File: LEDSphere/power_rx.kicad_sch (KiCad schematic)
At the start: 46 parts, among them U10 DRV5032FCDBZR, U3 TPS54202HDDCR, U4 TPS54202HDDCR

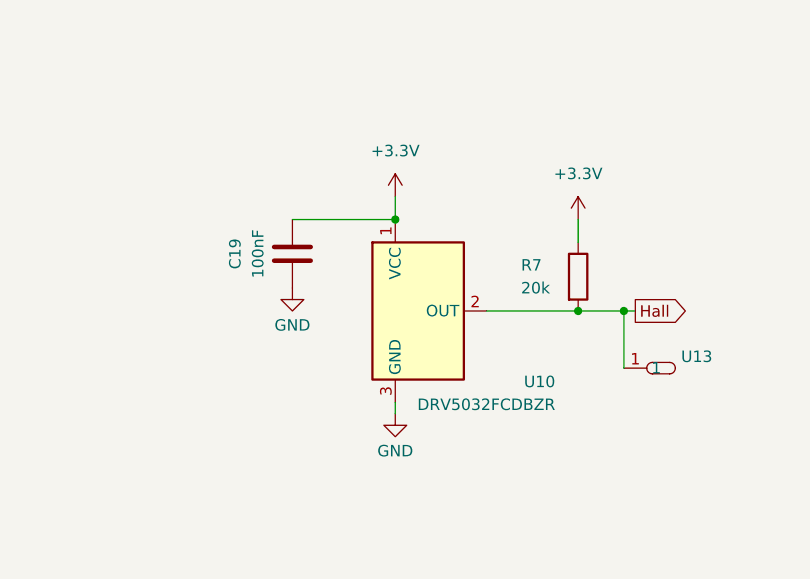
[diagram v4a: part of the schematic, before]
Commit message: change hall effect sensor
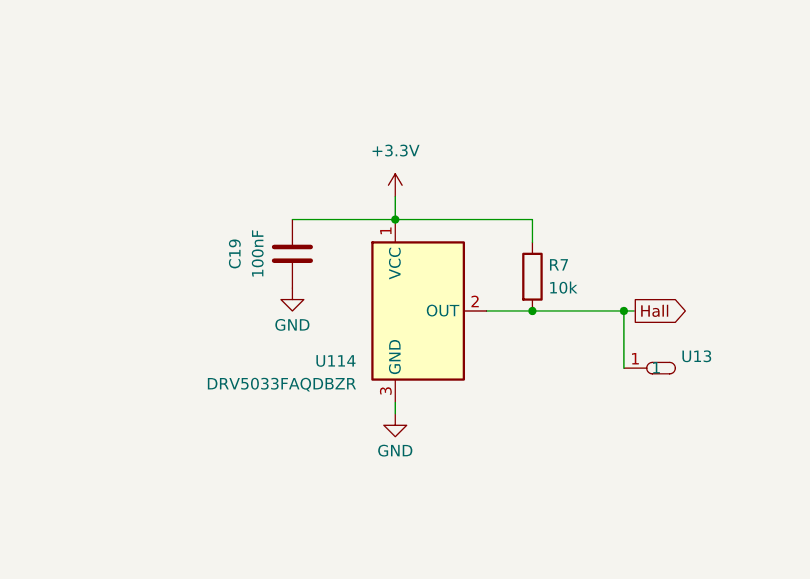
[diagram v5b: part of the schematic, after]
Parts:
- removed U10: DRV5032FCDBZR, Package_TO_SOT_SMD:SOT-23, symbol Sensor_Magnetic:DRV5033AJxDBZ
- added U114: DRV5033FAQDBZR, Package_TO_SOT_SMD:SOT-23-3, symbol Sensor_Magnetic:DRV5033FAxDBZ
- R7: value 20k -> 10k
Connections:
- net +3.3V: now also U114.1 (VCC)
- net GND: now also U114.3 (GND)
- net Hall: now also U114.2 (OUT)
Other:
- moved on the sheet: R7
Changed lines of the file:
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@@
 	)
 	(junction
+		(at 242.57 121.92)
+		(diameter 0)
+		(color 0 0 0 0)
+	)
+	(junction
 		(at 85.09 50.8)
 		(diameter 0)
@@
 	)
 	(junction
-		(at 247.65 121.92)
-		(diameter 0)
-		(color 0 0 0 0)
-	)
-	(junction
 		(at 158.75 162.56)
 		(diameter 0)
@@
 	(wire
 		(pts
+			(xy 237.49 121.92) (xy 242.57 121.92)
+		)
+		(stroke
+			(width 0)
+			(type default)
+		)
+	)
+	(wire
+		(pts
 			(xy 166.37 161.29) (xy 166.37 162.56)
 		)
@@
 	(wire
 		(pts
-			(xy 247.65 121.92) (xy 252.73 121.92)
+			(xy 99.06 52.07) (xy 81.28 52.07)
 		)
 		(stroke
@@
 	(wire
 		(pts
-			(xy 99.06 52.07) (xy 81.28 52.07)
+			(xy 99.06 50.8) (xy 99.06 52.07)
 		)
 		(stroke
@@
 	(wire
 		(pts
-			(xy 99.06 50.8) (xy 99.06 52.07)
+			(xy 227.33 109.22) (xy 227.33 111.76)
 		)
 		(stroke
@@
 	(wire
 		(pts
-			(xy 227.33 109.22) (xy 227.33 111.76)
+			(xy 227.33 111.76) (xy 242.57 111.76)
 		)
 		(stroke
@@
 	(wire
 		(pts
-			(xy 123.19 54.61) (xy 123.19 60.96)
+			(xy 242.57 121.92) (xy 252.73 121.92)
 		)
 		(stroke
@@
 	(wire
 		(pts
-			(xy 227.33 133.35) (xy 227.33 132.08)
+			(xy 123.19 54.61) (xy 123.19 60.96)
 		)
 		(stroke
@@
 	(wire
 		(pts
-			(xy 142.24 115.57) (xy 138.43 115.57)
+			(xy 227.33 133.35) (xy 227.33 132.08)
 		)
 		(stroke
@@
 	(wire
 		(pts
-			(xy 165.1 106.68) (xy 165.1 114.3)
+			(xy 142.24 115.57) (xy 138.43 115.57)
 		)
 		(stroke
@@
 	(wire
 		(pts
-			(xy 45.72 154.94) (xy 59.69 154.94)
+			(xy 165.1 106.68) (xy 165.1 114.3)
 		)
 		(stroke
@@
 	(wire
 		(pts
-			(xy 139.7 171.45) (xy 139.7 170.18)
+			(xy 45.72 154.94) (xy 59.69 154.94)
 		)
 		(stroke
@@
 	(wire
 		(pts
-			(xy 123.19 43.18) (xy 123.19 46.99)
+			(xy 139.7 171.45) (xy 139.7 170.18)
 		)
 		(stroke
@@
 	(wire
 		(pts
-			(xy 252.73 121.92) (xy 254 121.92)
+			(xy 123.19 43.18) (xy 123.19 46.99)
 		)
 		(stroke
@@
 	(wire
 		(pts
-			(xy 237.49 121.92) (xy 247.65 121.92)
+			(xy 252.73 121.92) (xy 254 121.92)
 		)
 		(stroke
@@
 	(wire
 		(pts
-			(xy 247.65 111.76) (xy 247.65 114.3)
+			(xy 242.57 111.76) (xy 242.57 114.3)
 		)
 		(stroke
@@
 	(symbol
 		(lib_id "Device:R")
-		(at 247.65 118.11 0)
+		(at 242.57 118.11 0)
 		(unit 1)
 		(body_style 1)
@@
 		(dnp no)
 		(property "Reference" "R7"
-			(at 241.3 116.84 0)
+			(at 244.348 116.84 0)
 			(show_name no)
 			(do_not_autoplace no)
@@
 			)
 		)
-		(property "Value" "20k"
-			(at 241.3 119.38 0)
+		(property "Value" "10k"
+			(at 244.348 119.38 0)
 			(show_name no)
 			(do_not_autoplace no)
@@
 		)
 		(property "Footprint" "Resistor_SMD:R_0603_1608Metric"
-			(at 245.872 118.11 90)
+			(at 240.792 118.11 90)
 			(hide yes)
 			(show_name no)
@@
 		)
 		(property "Datasheet" ""
-			(at 247.65 118.11 0)
+			(at 242.57 118.11 0)
 			(hide yes)
 			(show_name no)
@@
 		)
 		(property "Description" ""
-			(at 247.65 118.11 0)
+			(at 242.57 118.11 0)
 			(hide yes)
 			(show_name no)
@@
 		)
 		(property "LCSC" "C25765"
-			(at 247.65 118.11 90)
+			(at 242.57 118.11 90)
 			(hide yes)
 			(show_name no)
@@
 	)
 	(symbol
+		(lib_id "Sensor_Magnetic:DRV5033FAxDBZ")
+		(at 229.87 121.92 0)
+		(unit 1)
+		(body_style 1)
+		(exclude_from_sim no)
+		(in_bom yes)
+		(on_board yes)
+		(in_pos_files yes)
+		(dnp no)
+		(property "Reference" "U114"
+			(at 223.012 127.508 0)
+			(show_name no)
+			(do_not_autoplace no)
+			(effects
+				(font
+					(size 1.27 1.27)
+				)
+				(justify right)
+			)
+		)
+		(property "Value" "DRV5033FAQDBZR"
+			(at 223.012 130.048 0)
+			(show_name no)
+			(do_not_autoplace no)
+			(effects
+				(font
+					(size 1.27 1.27)
+				)
+				(justify right)
+			)
+		)
+		(property "Footprint" "Package_TO_SOT_SMD:SOT-23-3"
+			(at 229.87 121.92 0)
+			(hide yes)
+			(show_name no)
+			(do_not_autoplace no)
+			(effects
+				(font
+					(size 1.27 1.27)
+				)
+			)
+		)
+		(property "Datasheet" "https://www.ti.com/lit/ds/symlink/drv5033.pdf?ts=1775608513005"
+			(at 229.87 121.92 0)
+			(hide yes)
+			(show_name no)
+			(do_not_autoplace no)
+			(effects
+				(font
+					(size 1.27 1.27)
+				)
+			)
+		)
+		(property "Description" "±3.5 / ±2 mT, 20-kHz, 2-38V, SOT-23"
+			(at 229.87 121.92 0)
+			(hide yes)
+			(show_name no)
+			(do_not_autoplace no)
+			(effects
+				(font
+					(size 1.27 1.27)
+				)
+			)
+		)
+		(pin "3"
+		)
+		(pin "2"
+		)
+		(pin "1"
+		)
+		(instances
+			(project "power_rx"
+				(path "/ddd18393-06be-4266-b885-a3f36c5c5ced"
+					(reference "U114")
+					(unit 1)
+				)
+			)
+		)
+	)
+	(symbol
 		(lib_id "Device:C")
 		(at 44.45 102.87 180)
@@
 	)
 	(symbol
-		(lib_id "Sensor_Magnetic:DRV5033AJxDBZ")
-		(at 229.87 121.92 0)
-		(unit 1)
-		(body_style 1)
-		(exclude_from_sim no)
-		(in_bom yes)
-		(on_board yes)
-		(in_pos_files yes)
-		(dnp no)
-		(property "Reference" "U10"
-			(at 245.11 129.794 0)
-			(show_name no)
-			(do_not_autoplace no)
-			(effects
-				(font
-					(size 1.27 1.27)
-				)
-				(justify right)
-			)
-		)
-		(property "Value" "DRV5032FCDBZR"
-			(at 245.11 132.334 0)
-			(show_name no)
-			(do_not_autoplace no)
-			(effects
-				(font
-					(size 1.27 1.27)
-				)
-				(justify right)
-			)
-		)
-		(property "Footprint" "Package_TO_SOT_SMD:SOT-23"
-			(at 229.87 121.92 0)
-			(hide yes)
-			(show_name no)
-			(do_not_autoplace no)
-			(effects
-				(font
-					(size 1.27 1.27)
-				)
-			)
-		)
-		(property "Datasheet" "https://www.ti.com/lit/ds/symlink/drv5032.pdf?HQS=dis-dk-null-digikeymode-dsf-pf-null-wwe&ts=1774527949559&ref_url=https%253A%252F%252Fwww.ti.com%252Fgeneral%252Fdocs%252Fsuppproductinfo.tsp%253FdistId%253D10%2526gotoUrl%253Dhttps%253A%252F%252Fwww.ti.com%252Flit%252Fgpn%252Fdrv5032"
-			(at 229.87 121.92 0)
-			(hide yes)
-			(show_name no)
-			(do_not_autoplace no)
-			(effects
-				(font
-					(size 1.27 1.27)
-				)
-			)
-		)
-		(property "Description" "±4.8 / ±0.5 mT, 20-kHz, 2-38V, SOT-23"
-			(at 229.87 121.92 0)
-			(hide yes)
-			(show_name no)
-			(do_not_autoplace no)
-			(effects
-				(font
-					(size 1.27 1.27)
-				)
-			)
-		)
-		(pin "2"
-		)
-		(pin "1"
-		)
-		(pin "3"
-		)
-		(instances
-			(project "power_rx"
-				(path "/ddd18393-06be-4266-b885-a3f36c5c5ced"
-					(reference "U10")
-					(unit 1)
-				)
-			)
-		)
-	)
-	(symbol
 		(lib_id "power:GND")
 		(at 215.9 119.38 0)
@@
 					(unit 1)
 				)
-			)
-		)
-	)
-	(symbol
-		(lib_id "power:+3.3V")
-		(at 247.65 111.76 0)
-		(unit 1)
-		(body_style 1)
-		(exclude_from_sim no)
-		(in_bom yes)
-		(on_board yes)
-		(in_pos_files yes)
-		(dnp no)
-		(fields_autoplaced yes)
-		(property "Reference" "#PWR022"
-			(at 247.65 115.57 0)
-			(hide yes)
-			(show_name no)
-			(do_not_autoplace no)
-			(effects
-				(font
-					(size 1.27 1.27)
-				)
-			)
-		)
-		(property "Value" "+3.3V"
-			(at 247.65 106.68 0)
-			(show_name no)
-			(do_not_autoplace no)
-			(effects
-				(font
-					(size 1.27 1.27)
-				)
-			)
-		)
-		(property "Footprint" ""
-			(at 247.65 111.76 0)
-			(hide yes)
-			(show_name no)
-			(do_not_autoplace no)
-			(effects
-				(font
-					(size 1.27 1.27)
-				)
-			)
-		)
-		(property "Datasheet" ""
-			(at 247.65 111.76 0)
-			(hide yes)
-			(show_name no)
-			(do_not_autoplace no)
-			(effects
-				(font
-					(size 1.27 1.27)
-				)
-			)
-		)
-		(property "Description" ""
-			(at 247.65 111.76 0)
-			(hide yes)
-			(show_name no)
-			(do_not_autoplace no)
-			(effects
-				(font
-					(size 1.27 1.27)
-				)
-			)
-		)
-		(pin "1"
-		)
-		(instances
-			(project "power_rx"
-				(path "/ddd18393-06be-4266-b885-a3f36c5c5ced"
-					(reference "#PWR022")
-					(unit 1)
-				)

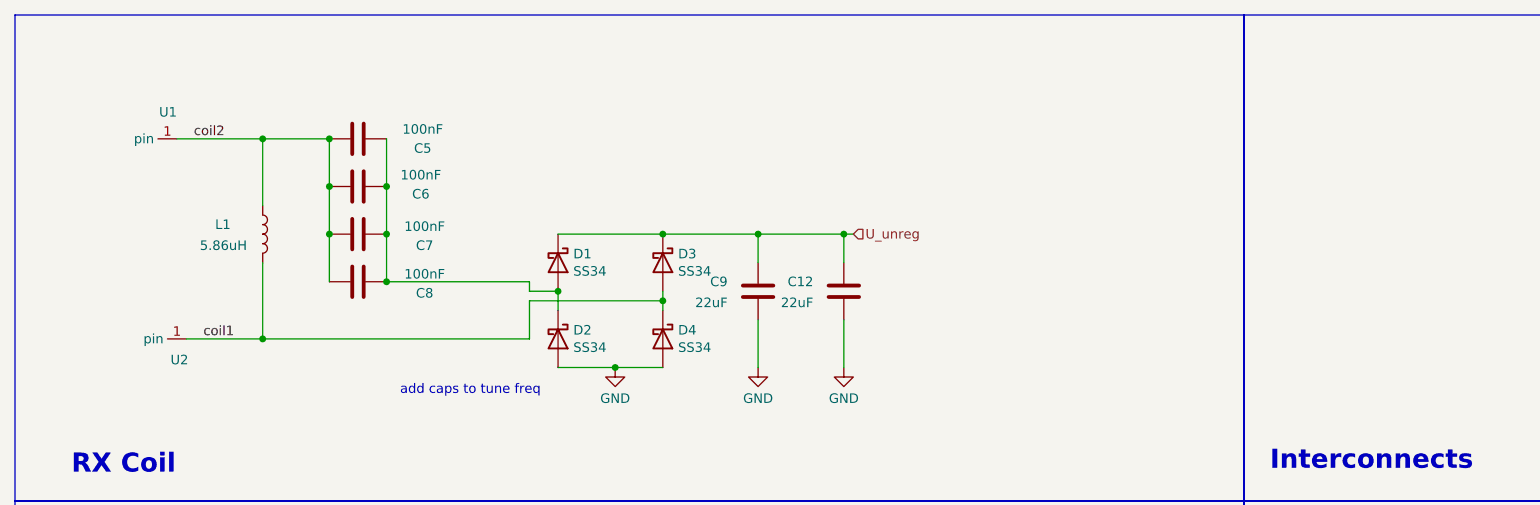
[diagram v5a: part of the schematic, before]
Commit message: change power rx gnding, add step files of all boards
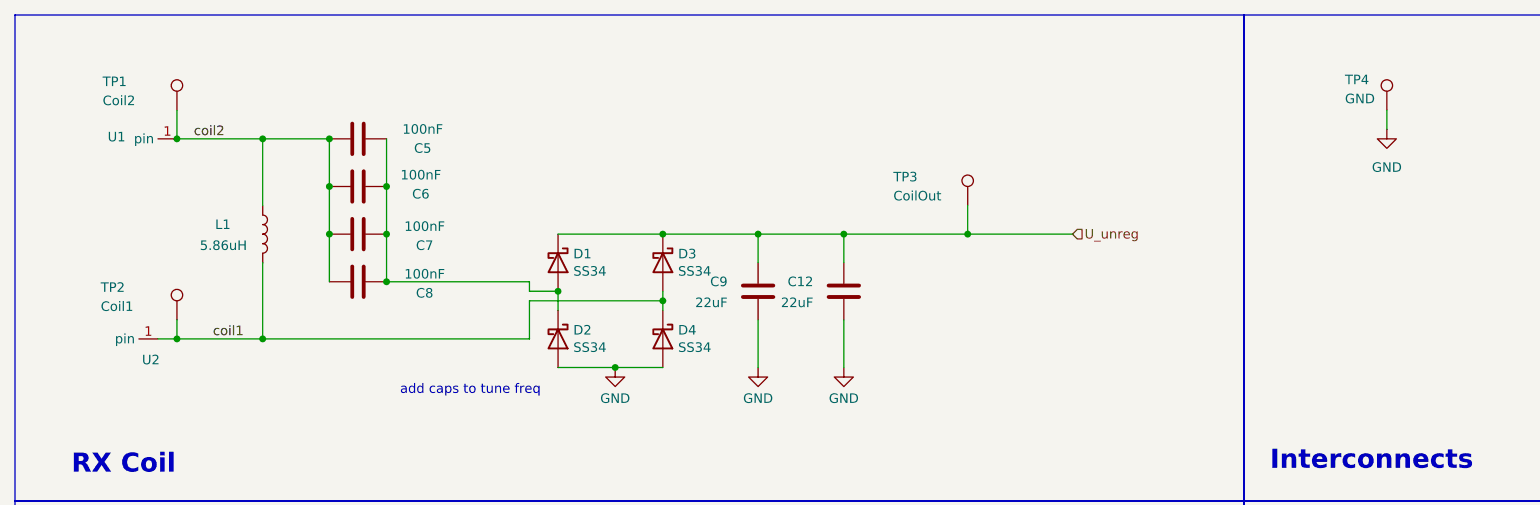
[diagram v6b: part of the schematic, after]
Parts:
- added TP1: Coil2, TestPoint:TestPoint_THTPad_D2.0mm_Drill1.0mm, symbol Connector:TestPoint
- added TP2: Coil1, TestPoint:TestPoint_THTPad_D2.0mm_Drill1.0mm, symbol Connector:TestPoint
- added TP3: CoilOut, TestPoint:TestPoint_THTPad_D2.0mm_Drill1.0mm, symbol Connector:TestPoint
- added TP4: GND, TestPoint:TestPoint_THTPad_D2.0mm_Drill1.0mm, symbol Connector:TestPoint
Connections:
- net GND: now also TP4.1
- net U_unreg: now also TP3.1
- net coil1: now also TP2.1
- net coil2: now also TP1.1
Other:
- moved on the sheet: U2

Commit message: adjust test point
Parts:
- TP1, TP2: footprint TestPoint:TestPoint_THTPad_D2.0mm_Drill1.0mm -> TestPoint:TestPoint_Pad_1.0x1.0mm
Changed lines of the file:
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@@
 			)
 		)
-		(property "Footprint" "TestPoint:TestPoint_THTPad_D2.0mm_Drill1.0mm"
+		(property "Footprint" "TestPoint:TestPoint_Pad_1.0x1.0mm"
 			(at 39.37 54.61 0)
 			(hide yes)
@@
 			)
 		)
-		(property "Footprint" "TestPoint:TestPoint_THTPad_D2.0mm_Drill1.0mm"
+		(property "Footprint" "TestPoint:TestPoint_Pad_1.0x1.0mm"
 			(at 39.37 26.67 0)
 			(hide yes)

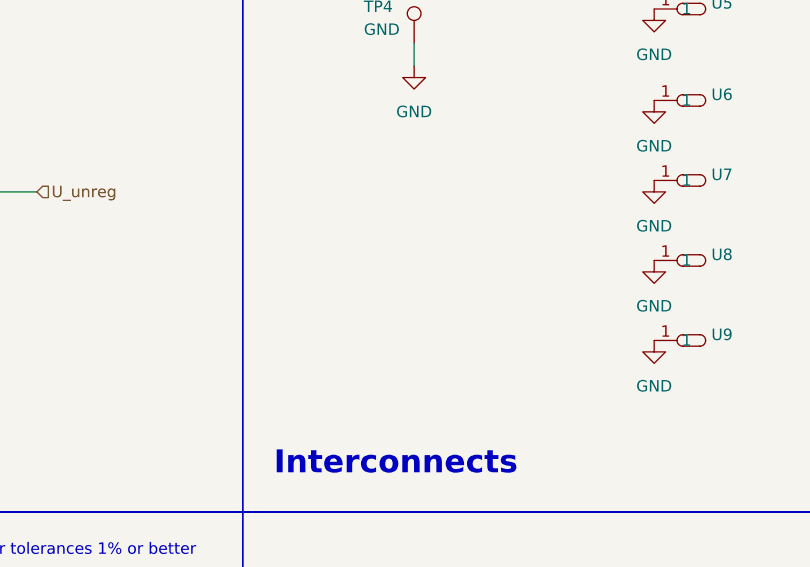
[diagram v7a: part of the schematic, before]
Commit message: alter rx to avoid flux lines
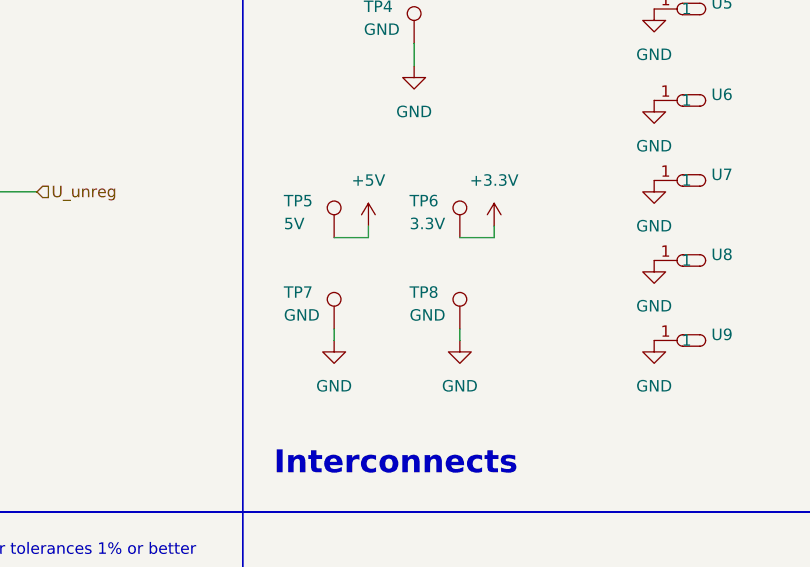
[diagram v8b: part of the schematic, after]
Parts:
- added TP5: 5V, TestPoint:TestPoint_Pad_1.0x1.0mm, symbol Connector:TestPoint
- added TP6: 3.3V, TestPoint:TestPoint_Pad_1.0x1.0mm, symbol Connector:TestPoint
- added TP7, TP8: GND, TestPoint:TestPoint_Pad_1.0x1.0mm, symbol Connector:TestPoint
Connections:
- net +3.3V: now also TP6.1
- net +5V: now also TP5.1
- net GND: now also TP7.1, TP8.1
